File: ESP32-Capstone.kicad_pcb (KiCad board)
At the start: 2 copper layers, 1 part, among them IC1 ESP32-C3FN4

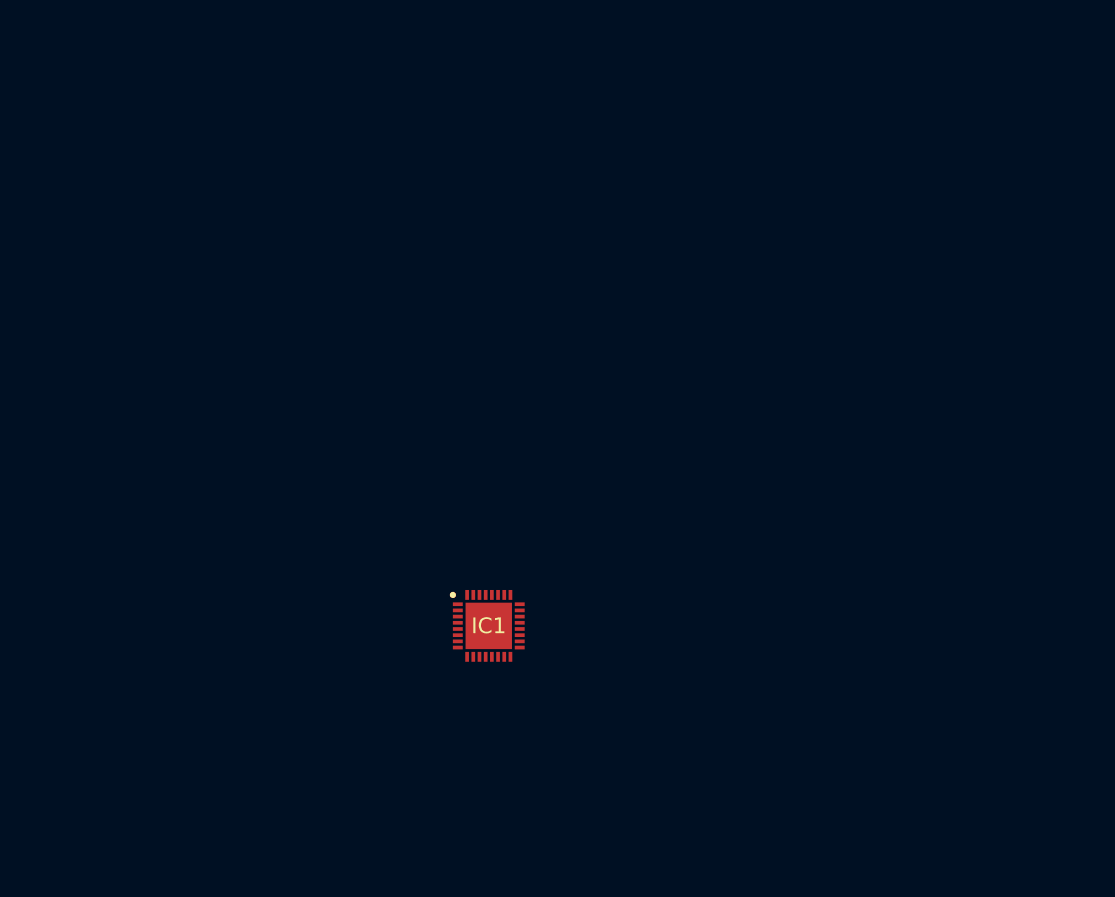
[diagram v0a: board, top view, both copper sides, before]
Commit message: fix: update schematic picture
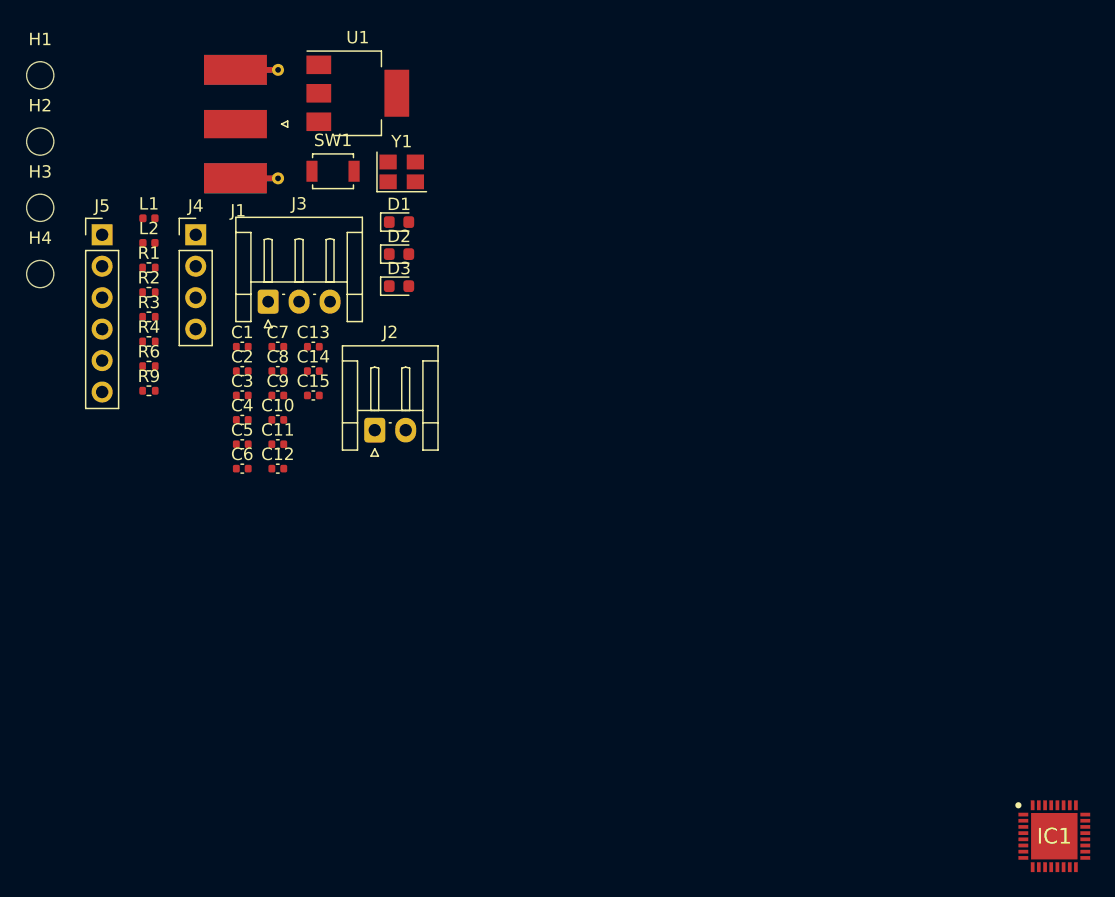
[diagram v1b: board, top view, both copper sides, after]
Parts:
- added C1: 100n, Capacitor_SMD:C_0402_1005Metric, F.Cu at (84.3, 51.9)
- added C10: 15p, Capacitor_SMD:C_0402_1005Metric, F.Cu at (87.1, 57.8)
- added C11: 100n, Capacitor_SMD:C_0402_1005Metric, F.Cu at (87.1, 59.8)
- added C12: 10u, Capacitor_SMD:C_0402_1005Metric, F.Cu at (87.1, 61.8)
- added C13: 10u, Capacitor_SMD:C_0402_1005Metric, F.Cu at (90.0, 51.9)
- added C14: 3p3, Capacitor_SMD:C_0402_1005Metric, F.Cu at (90.0, 53.9)
- added C15: 3p3, Capacitor_SMD:C_0402_1005Metric, F.Cu at (90.0, 55.8)
- added C2: 100n, Capacitor_SMD:C_0402_1005Metric, F.Cu at (84.3, 53.9)
- added C3: 1u, Capacitor_SMD:C_0402_1005Metric, F.Cu at (84.3, 55.8)
- added C4: 10u, Capacitor_SMD:C_0402_1005Metric, F.Cu at (84.3, 57.8)
- added C5: 100n, Capacitor_SMD:C_0402_1005Metric, F.Cu at (84.3, 59.8)
- added C6: 100n, Capacitor_SMD:C_0402_1005Metric, F.Cu at (84.3, 61.8)
- added C7: 10u, Capacitor_SMD:C_0402_1005Metric, F.Cu at (87.1, 51.9)
- added C8: 100n, Capacitor_SMD:C_0402_1005Metric, F.Cu at (87.1, 53.9)
- added C9: 15p, Capacitor_SMD:C_0402_1005Metric, F.Cu at (87.1, 55.8)
- added D1: GREEN, LED_SMD:LED_0603_1608Metric, F.Cu at (96.9, 41.8)
- added D2: YELLOW, LED_SMD:LED_0603_1608Metric, F.Cu at (96.9, 44.4)
- added D3: BLUE, LED_SMD:LED_0603_1608Metric, F.Cu at (96.9, 47.0)
- added H1: MountingHole, MountingHole:MountingHole_2.2mm_M2_ISO14580, F.Cu at (68.0, 30.0)
- added H2: MountingHole, MountingHole:MountingHole_2.2mm_M2_ISO14580, F.Cu at (68.0, 35.3)
- added H3: MountingHole, MountingHole:MountingHole_2.2mm_M2_ISO14580, F.Cu at (68.0, 40.7)
- added H4: MountingHole, MountingHole:MountingHole_2.2mm_M2_ISO14580, F.Cu at (68.0, 46.0)
- added J1: SMA_CONN, Connector_Coaxial:SMA_Molex_73251-1153_EdgeMount_Horizontal, F.Cu at (85.4, 33.9)
- added J2: BATTERY, Connector_JST:JST_EH_S2B-EH_1x02_P2.50mm_Horizontal, F.Cu at (95.0, 58.6)
- added J3: SENSOR, Connector_JST:JST_EH_S3B-EH_1x03_P2.50mm_Horizontal, F.Cu at (86.4, 48.3)
- added J4: UART, Connector_PinHeader_2.54mm:PinHeader_1x04_P2.54mm_Vertical, F.Cu at (80.5, 42.9)
- added J5: JTAG, Connector_PinHeader_2.54mm:PinHeader_1x06_P2.54mm_Vertical, F.Cu at (73.0, 42.9)
- added L1: 2n2, Inductor_SMD:L_0402_1005Metric, F.Cu at (76.7, 41.5)
- added L2: 2n2, Inductor_SMD:L_0402_1005Metric, F.Cu at (76.7, 43.5)
- added R1: 22R, Resistor_SMD:R_0402_1005Metric, F.Cu at (76.7, 45.5)
- added R2: 5k1, Resistor_SMD:R_0402_1005Metric, F.Cu at (76.7, 47.5)
- added R3: 1k, Resistor_SMD:R_0402_1005Metric, F.Cu at (76.7, 49.5)
- added R4: 1k, Resistor_SMD:R_0402_1005Metric, F.Cu at (76.7, 51.5)
- added R6: 1k, Resistor_SMD:R_0402_1005Metric, F.Cu at (76.7, 53.5)
- added R9: 499, Resistor_SMD:R_0402_1005Metric, F.Cu at (76.7, 55.5)
- added SW1: SW_SPST, Button_Switch_SMD:SW_SPST_B3U-1000P, F.Cu at (91.6, 37.7)
- added U1: AMS1117-3.3, Package_TO_SOT_SMD:SOT-223-3_TabPin2, F.Cu at (93.6, 31.4)
- added Y1: 40MHz, Crystal:Crystal_SMD_SeikoEpson_FA238-4Pin_3.2x2.5mm, F.Cu at (97.2, 37.8)
- moved IC1 48.7 mm to (149.9, 91.4)
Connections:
- IC1 pad 1: unconnected-(IC1-LNA_IN-Pad1) -> /LNA_IN
- IC1 pad 10: unconnected-(IC1-MTDI-Pad10) -> /MTDI
- IC1 pad 11: unconnected-(IC1-VDD3P3_RTC-Pad11) -> +3V3
- IC1 pad 12: unconnected-(IC1-MTCK-Pad12) -> /MTCK
- IC1 pad 13: unconnected-(IC1-MTDO-Pad13) -> /MTDO
- IC1 pad 14: unconnected-(IC1-GPIO8-Pad14) -> /LED_OUT_1
- IC1 pad 15: unconnected-(IC1-GPIO9-Pad15) -> /LED_OUT_2
- IC1 pad 17: unconnected-(IC1-VDD3P3_CPU-Pad17) -> +3V3
- IC1 pad 18: unconnected-(IC1-VDD_SPI-Pad18) -> +3V3
- IC1 pad 2: unconnected-(IC1-VDD3P3_1-Pad2) -> Net-(IC1-VDD3P3_1)
- IC1 pad 27: unconnected-(IC1-U0RXD-Pad27) -> /UART0_RX
- IC1 pad 28: unconnected-(IC1-U0TXD-Pad28) -> Net-(IC1-U0TXD)
- IC1 pad 29: unconnected-(IC1-XTAL_N-Pad29) -> /XTAL_N
- IC1 pad 3: unconnected-(IC1-VDD3P3_2-Pad3) -> Net-(IC1-VDD3P3_1)
- IC1 pad 30: unconnected-(IC1-XTAL_P-Pad30) -> /XTAL_P
- IC1 pad 31: unconnected-(IC1-VDDA_1-Pad31) -> +3V3
- IC1 pad 32: unconnected-(IC1-VDDA_2-Pad32) -> +3V3
- IC1 pad 33: unconnected-(IC1-EP-Pad33) -> GND
- IC1 pad 7: unconnected-(IC1-CHIP_EN-Pad7) -> /CHIP_EN
- IC1 pad 8: unconnected-(IC1-GPIO3-Pad8) -> /SENSOR_IN
- IC1 pad 9: unconnected-(IC1-MTMS-Pad9) -> /MTMS
